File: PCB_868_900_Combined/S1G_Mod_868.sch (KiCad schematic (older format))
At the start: 63 parts, among them Q1 DMG2307L-7, SW1 CUS-12TB, T1 0732511150, U1 AP7361-33FGE-7, U2 ADF7023BCPZ, X1 ABS05-32.768KHZ-9-T, X2 ABM11-140-26.000MHZ-T3

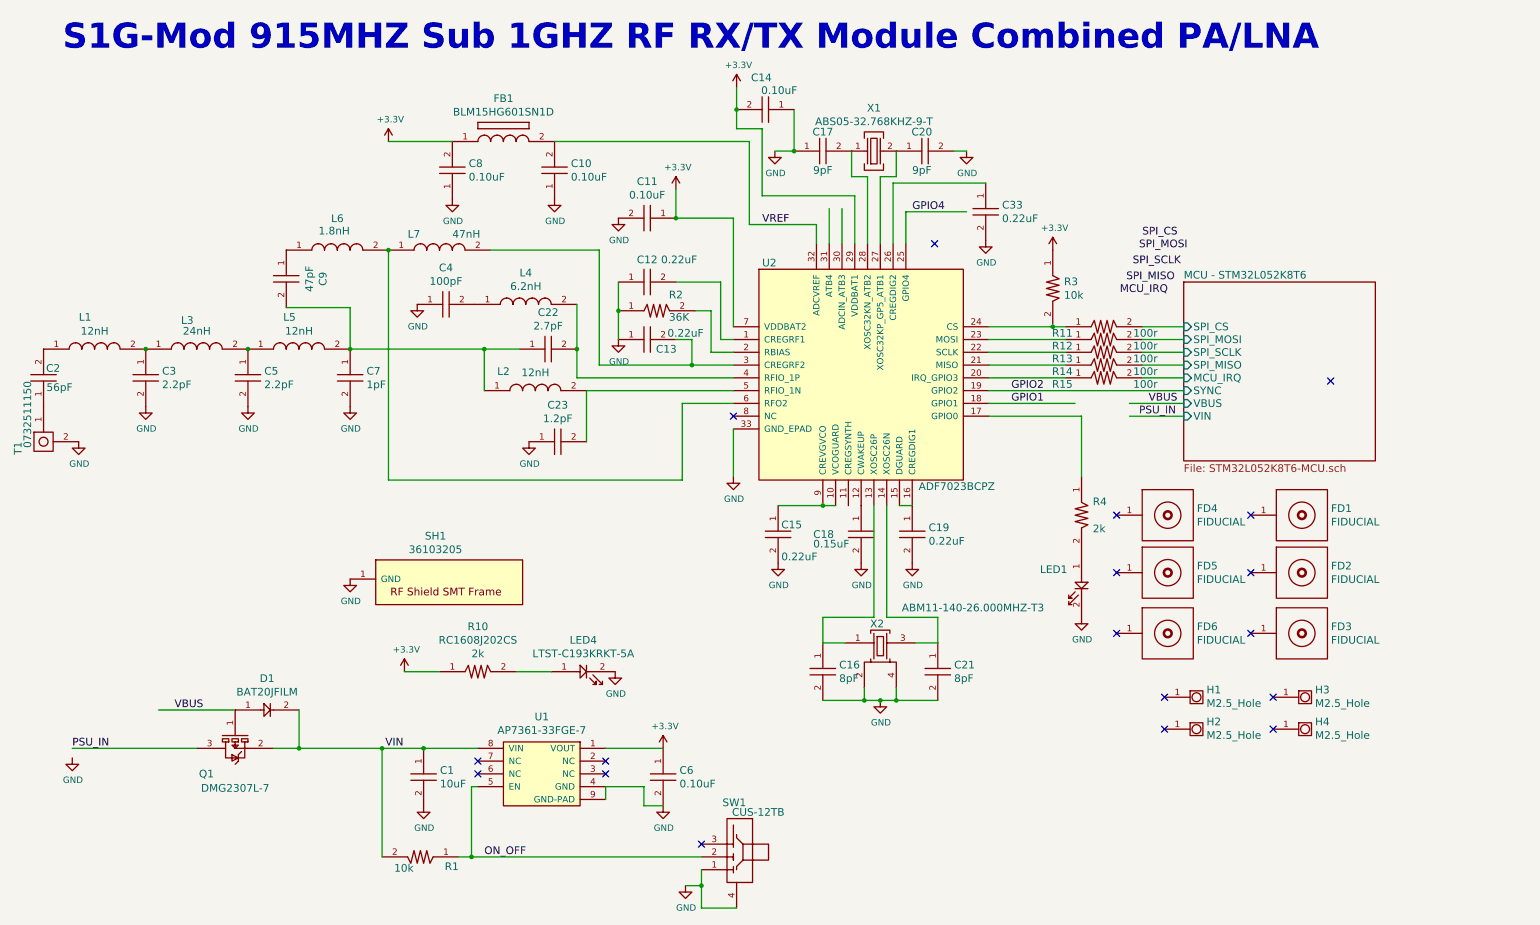
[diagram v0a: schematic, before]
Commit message: Radio Reference Schematic Errors
Some errors transcribing ADI's reference shcematic. 0.22uF caps added to
pins that needed it etc.
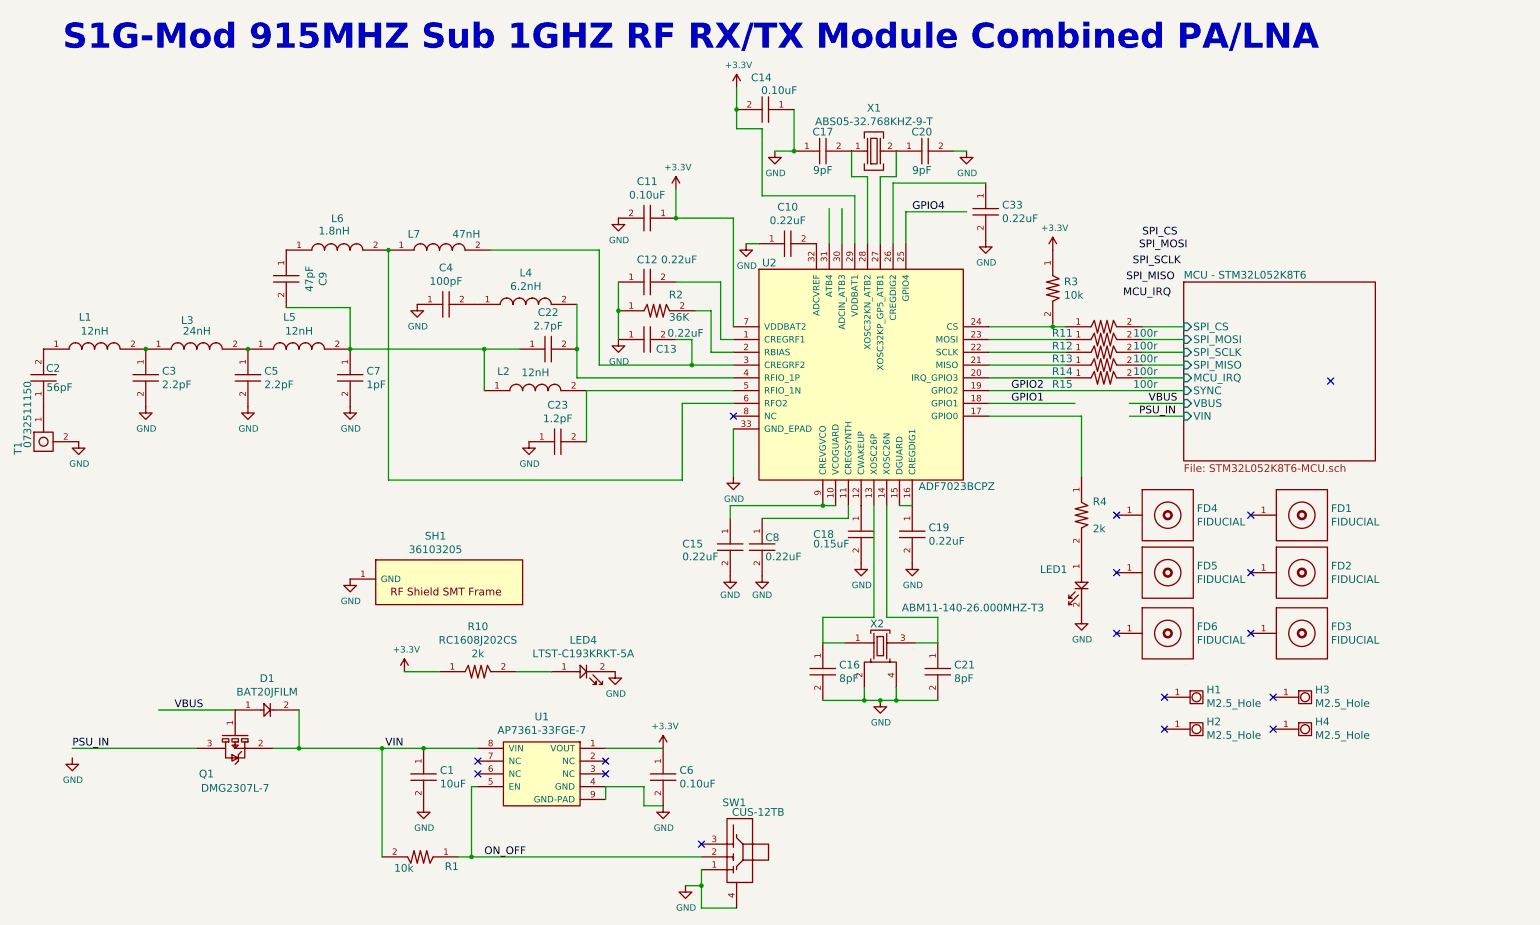
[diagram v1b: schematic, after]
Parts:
- removed C10, C8: CL05B104JP5NNNC, PCB_Footprints:C0402, symbol CL05B104JP5NNNC
- removed FB1: BLM15HG601SN1D, PCB_Footprints:BLM15HG601SN1D, symbol BLM15HG601SN1D
- added C10, C8: CL05A224KP5NNNC, PCB_Footprints:C0402, symbol CL05A224KP5NNNC
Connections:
- net labels removed: VREF
- wire segments 100 -> 99
- no-connect marks 18 -> 17
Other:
- moved on the sheet: C15

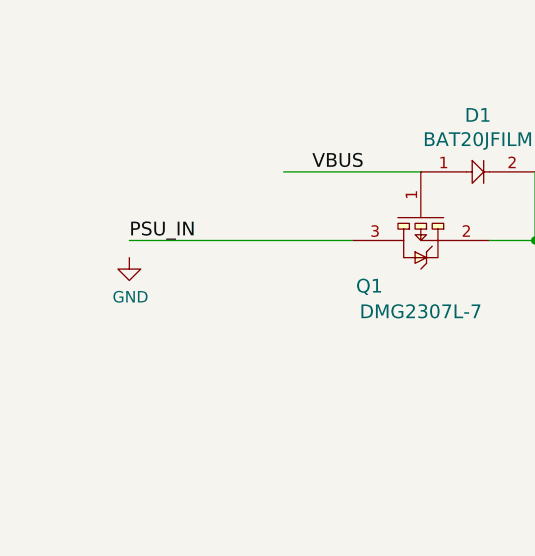
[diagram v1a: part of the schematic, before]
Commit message: PDF
schematic exported as color PDF for review
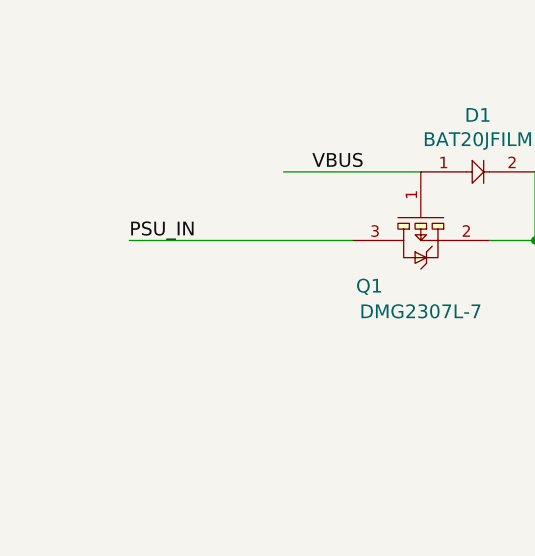
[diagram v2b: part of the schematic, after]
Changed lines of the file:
@@
 $EndComp
 $Comp
-L GND #PWR25
+L GND #PWR01
 U 1 1 58161058
 P 7275 6075
-F 0 "#PWR25" H 7275 5825 50  0001 C CNN
+F 0 "#PWR01" H 7275 5825 50  0001 C CNN
 F 1 "GND" H 7280 5902 50  0000 C CNN
 F 2 "" H 7275 6075 50  0000 C CNN
@@
 $EndComp
 $Comp
-L GND #PWR19
+L GND #PWR02
 U 1 1 5816222C
 P 6125 4325
-F 0 "#PWR19" H 6125 4075 50  0001 C CNN
+F 0 "#PWR02" H 6125 4075 50  0001 C CNN
 F 1 "GND" H 6130 4152 50  0000 C CNN
 F 2 "" H 6125 4325 50  0000 C CNN
@@
 $EndComp
 $Comp
-L +3.3V #PWR16
+L +3.3V #PWR03
 U 1 1 581623E1
 P 5675 2075
-F 0 "#PWR16" H 5675 1925 50  0001 C CNN
+F 0 "#PWR03" H 5675 1925 50  0001 C CNN
 F 1 "+3.3V" H 5690 2248 50  0000 C CNN
 F 2 "" H 5675 2075 50  0000 C CNN
@@
 $EndComp
 $Comp
-L GND #PWR13
+L GND #PWR04
 U 1 1 58162F98
 P 5225 3250
-F 0 "#PWR13" H 5225 3000 50  0001 C CNN
+F 0 "#PWR04" H 5225 3000 50  0001 C CNN
 F 1 "GND" H 5230 3077 50  0000 C CNN
 F 2 "" H 5225 3250 50  0000 C CNN
@@
 $EndComp
 $Comp
-L GND #PWR18
+L GND #PWR05
 U 1 1 58164E94
 P 6100 5100
-F 0 "#PWR18" H 6100 4850 50  0001 C CNN
+F 0 "#PWR05" H 6100 4850 50  0001 C CNN
 F 1 "GND" H 6100 4950 50  0000 C CNN
 F 2 "" H 6100 5100 50  0000 C CNN
@@
 $EndComp
 $Comp
-L GND #PWR26
+L GND #PWR06
 U 1 1 58165059
 P 7525 5000
-F 0 "#PWR26" H 7525 4750 50  0001 C CNN
+F 0 "#PWR06" H 7525 4750 50  0001 C CNN
 F 1 "GND" H 7530 4827 50  0000 C CNN
 F 2 "" H 7525 5000 50  0000 C CNN
@@
 $EndComp
 $Comp
-L GND #PWR24
+L GND #PWR07
 U 1 1 58165567
 P 7125 5000
-F 0 "#PWR24" H 7125 4750 50  0001 C CNN
+F 0 "#PWR07" H 7125 4750 50  0001 C CNN
 F 1 "GND" H 7130 4827 50  0000 C CNN
 F 2 "" H 7125 5000 50  0000 C CNN
@@
 $EndComp
 $Comp
-L GND #PWR30
+L GND #PWR08
 U 1 1 58168376
 P 8850 5425
-F 0 "#PWR30" H 8850 5175 50  0001 C CNN
+F 0 "#PWR08" H 8850 5175 50  0001 C CNN
 F 1 "GND" H 8855 5252 50  0000 C CNN
 F 2 "" H 8850 5425 50  0000 C CNN
@@
 $EndComp
 $Comp
-L +3.3V #PWR20
+L +3.3V #PWR09
 U 1 1 58168986
 P 6150 1275
-F 0 "#PWR20" H 6150 1125 50  0001 C CNN
+F 0 "#PWR09" H 6150 1125 50  0001 C CNN
 F 1 "+3.3V" H 6165 1448 50  0000 C CNN
 F 2 "" H 6150 1275 50  0000 C CNN
@@
 $EndComp
 $Comp
-L GND #PWR12
+L GND #PWR010
 U 1 1 58169314
 P 5225 2300
-F 0 "#PWR12" H 5225 2050 50  0001 C CNN
+F 0 "#PWR010" H 5225 2050 50  0001 C CNN
 F 1 "GND" H 5230 2127 50  0000 C CNN
 F 2 "" H 5225 2300 50  0000 C CNN
@@
 $EndComp
 $Comp
-L GND #PWR3
+L GND #PWR011
 U 1 1 58174222
 P 1525 3775
-F 0 "#PWR3" H 1525 3525 50  0001 C CNN
+F 0 "#PWR011" H 1525 3525 50  0001 C CNN
 F 1 "GND" H 1530 3602 50  0000 C CNN
 F 2 "" H 1525 3775 50  0000 C CNN
@@
 $EndComp
 $Comp
-L GND #PWR4
+L GND #PWR012
 U 1 1 581744A7
 P 2325 3775
-F 0 "#PWR4" H 2325 3525 50  0001 C CNN
+F 0 "#PWR012" H 2325 3525 50  0001 C CNN
 F 1 "GND" H 2330 3602 50  0000 C CNN
 F 2 "" H 2325 3775 50  0000 C CNN
@@
 $EndComp
 $Comp
-L GND #PWR9
+L GND #PWR013
 U 1 1 5816BC64
 P 3700 6900
-F 0 "#PWR9" H 3700 6650 50  0001 C CNN
+F 0 "#PWR013" H 3700 6650 50  0001 C CNN
 F 1 "GND" H 3705 6727 50  0000 C CNN
 F 2 "" H 3700 6900 50  0000 C CNN
@@
 $EndComp
 $Comp
-L GND #PWR15
+L GND #PWR014
 U 1 1 5816BFC1
 P 5575 6900
-F 0 "#PWR15" H 5575 6650 50  0001 C CNN
+F 0 "#PWR014" H 5575 6650 50  0001 C CNN
 F 1 "GND" H 5580 6727 50  0000 C CNN
 F 2 "" H 5575 6900 50  0000 C CNN
@@
 $EndComp
 $Comp
-L +3.3V #PWR14
+L +3.3V #PWR015
 U 1 1 5816C55D
 P 5575 6450
-F 0 "#PWR14" H 5575 6300 50  0001 C CNN
+F 0 "#PWR015" H 5575 6300 50  0001 C CNN
 F 1 "+3.3V" H 5590 6623 50  0000 C CNN
 F 2 "" H 5575 6450 50  0000 C CNN
@@
 MCU_IRQ
 $Comp
-L GND #PWR23
+L GND #PWR016
 U 1 1 58175F58
 P 6450 1775
-F 0 "#PWR23" H 6450 1525 50  0001 C CNN
+F 0 "#PWR016" H 6450 1525 50  0001 C CNN
 F 1 "GND" H 6455 1602 50  0000 C CNN
 F 2 "" H 6450 1775 50  0000 C CNN
@@
 $EndComp
 $Comp
-L GND #PWR27
+L GND #PWR017
 U 1 1 581763CA
 P 7950 1775
-F 0 "#PWR27" H 7950 1525 50  0001 C CNN
+F 0 "#PWR017" H 7950 1525 50  0001 C CNN
 F 1 "GND" H 7955 1602 50  0000 C CNN
 F 2 "" H 7950 1775 50  0000 C CNN
@@
 $EndComp
 $Comp
-L GND #PWR5
+L GND #PWR018
 U 1 1 5818E84F
 P 3125 3775
-F 0 "#PWR5" H 3125 3525 50  0001 C CNN
+F 0 "#PWR018" H 3125 3525 50  0001 C CNN
 F 1 "GND" H 3130 3602 50  0000 C CNN
 F 2 "" H 3125 3775 50  0000 C CNN
@@
 $EndComp
 $Comp
-L GND #PWR10
+L GND #PWR019
 U 1 1 58195E9E
 P 4525 4050
-F 0 "#PWR10" H 4525 3800 50  0001 C CNN
+F 0 "#PWR019" H 4525 3800 50  0001 C CNN
 F 1 "GND" H 4530 3877 50  0000 C CNN
 F 2 "" H 4525 4050 50  0000 C CNN
@@
 $EndComp
 $Comp
-L GND #PWR8
+L GND #PWR020
 U 1 1 58196935
 P 3650 2975
-F 0 "#PWR8" H 3650 2725 50  0001 C CNN
+F 0 "#PWR020" H 3650 2725 50  0001 C CNN
 F 1 "GND" H 3655 2802 50  0000 C CNN
 F 2 "" H 3650 2975 50  0000 C CNN
@@
 $EndComp
 $Comp
-L GND #PWR2
+L GND #PWR021
 U 1 1 581979F7
 P 1000 4050
-F 0 "#PWR2" H 1000 3800 50  0001 C CNN
+F 0 "#PWR021" H 1000 3800 50  0001 C CNN
 F 1 "GND" H 1005 3877 50  0000 C CNN
 F 2 "" H 1000 4050 50  0000 C CNN
@@
 $EndComp
 $Comp
-L +3.3V #PWR29
+L +3.3V #PWR022
 U 1 1 581AA58C
 P 8625 2550
-F 0 "#PWR29" H 8625 2400 50  0001 C CNN
+F 0 "#PWR022" H 8625 2400 50  0001 C CNN
 F 1 "+3.3V" H 8640 2723 50  0000 C CNN
 F 2 "" H 8625 2550 50  0000 C CNN
@@
 NoConn ~ 10350 6050
 $Comp
-L GND #PWR17
+L GND #PWR023
 U 1 1 5822EA21
 P 5750 7525
-F 0 "#PWR17" H 5750 7275 50  0001 C CNN
+F 0 "#PWR023" H 5750 7275 50  0001 C CNN
 F 1 "GND" H 5755 7352 50  0000 C CNN
 F 2 "" H 5750 7525 50  0000 C CNN
@@
 F 20 "Diode Schottky 23V 1A Surface Mount SOD-323" H 3925 7950 60  0001 C CNN "Description"
 	1    2475 6150
-	1    0    0    -1
-$EndComp
-$Comp
-L GND #PWR1
-U 1 1 582360D6
-P 950 6525
-F 0 "#PWR1" H 950 6275 50  0001 C CNN
-F 1 "GND" H 955 6352 50  0000 C CNN
-F 2 "" H 950 6525 50  0000 C CNN
-F 3 "" H 950 6525 50  0000 C CNN
-	1    950  6525
 	1    0    0    -1
 $EndComp
@@
 	9225 3850 9650 3850
 $Comp
-L GND #PWR6
+L GND #PWR025
 U 1 1 5824D7CE
 P 3125 5125
-F 0 "#PWR6" H 3125 4875 50  0001 C CNN
+F 0 "#PWR025" H 3125 4875 50  0001 C CNN
 F 1 "GND" H 3130 4952 50  0000 C CNN
 F 2 "" H 3125 5125 50  0000 C CNN
@@
 	7375 2025 7375 2500
 $Comp
-L GND #PWR28
+L GND #PWR026
 U 1 1 582AA168
 P 8100 2475
-F 0 "#PWR28" H 8100 2225 50  0001 C CNN
+F 0 "#PWR026" H 8100 2225 50  0001 C CNN
 F 1 "GND" H 8105 2302 50  0000 C CNN
 F 2 "" H 8100 2475 50  0000 C CNN
@@
 $EndComp
 $Comp
-L GND #PWR11
+L GND #PWR027
 U 1 1 582B9301
 P 5200 5850
-F 0 "#PWR11" H 5200 5600 50  0001 C CNN
+F 0 "#PWR027" H 5200 5600 50  0001 C CNN
 F 1 "GND" H 5205 5677 50  0000 C CNN
 F 2 "" H 5200 5850 50  0000 C CNN
@@
 	4700 5850 4425 5850
 $Comp
-L +3.3V #PWR7
+L +3.3V #PWR028
 U 1 1 582B94B0
 P 3550 5850
-F 0 "#PWR7" H 3550 5700 50  0001 C CNN
+F 0 "#PWR028" H 3550 5700 50  0001 C CNN
 F 1 "+3.3V" H 3565 6023 50  0000 C CNN
 F 2 "" H 3550 5850 50  0000 C CNN
@@
 $EndComp
 $Comp
-L GND #PWR21
+L GND #PWR029
 U 1 1 596AE02D
 P 6225 2500
-F 0 "#PWR21" H 6225 2250 50  0001 C CNN
+F 0 "#PWR029" H 6225 2250 50  0001 C CNN
 F 1 "GND" H 6230 2327 50  0000 C CNN
 F 2 "" H 6225 2500 50  0000 C CNN
@@
 	6100 4650 6100 4550
 $Comp
-L GND #PWR22
+L GND #PWR030
 U 1 1 596BDD64
 P 6350 5100
-F 0 "#PWR22" H 6350 4850 50  0001 C CNN
+F 0 "#PWR030" H 6350 4850 50  0001 C CNN
 F 1 "GND" H 6350 4950 50  0000 C CNN
 F 2 "" H 6350 5100 50  0000 C CNN
